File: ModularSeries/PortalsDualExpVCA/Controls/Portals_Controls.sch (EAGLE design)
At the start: 15 parts, among them SW1 SPDT_SWITCHDW1, SW2 SPDT_SWITCHDW1

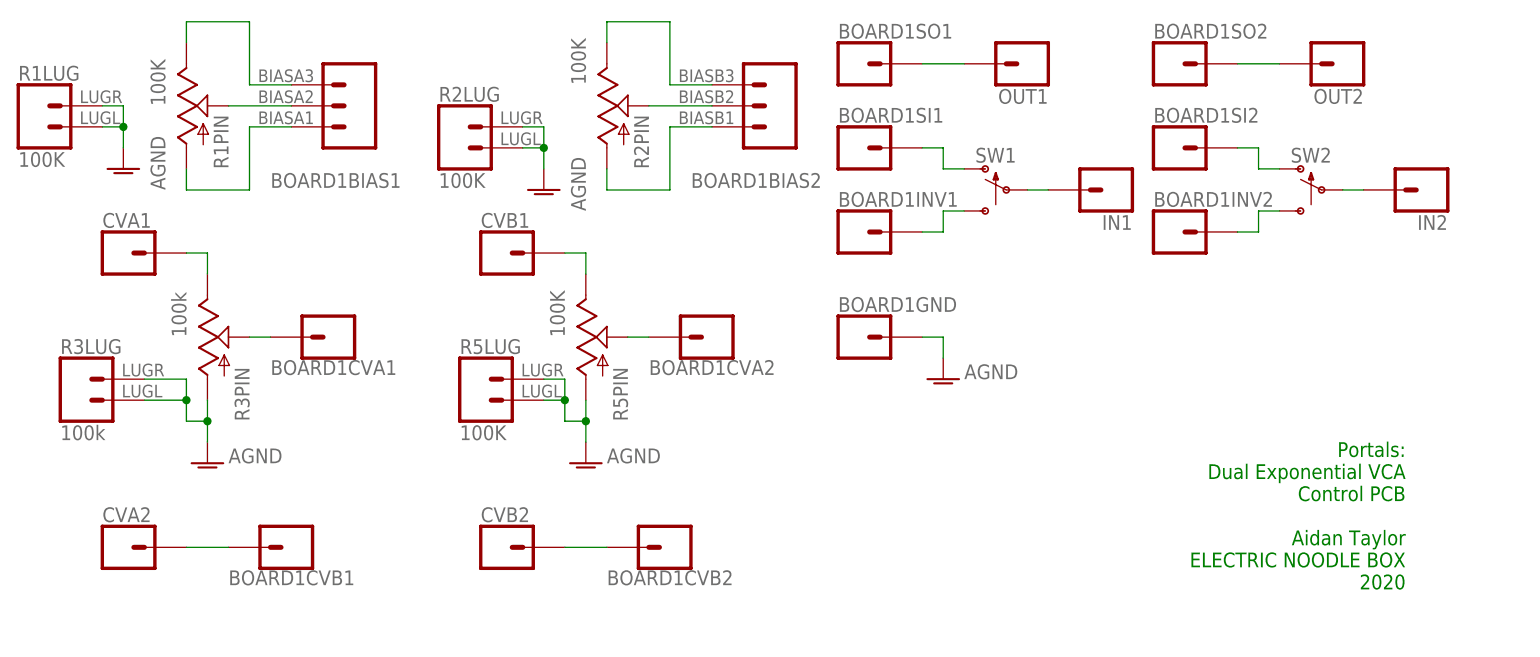
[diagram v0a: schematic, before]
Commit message: Pulse output fixed on Knives, schematics and layout updated. Panel added for Portals
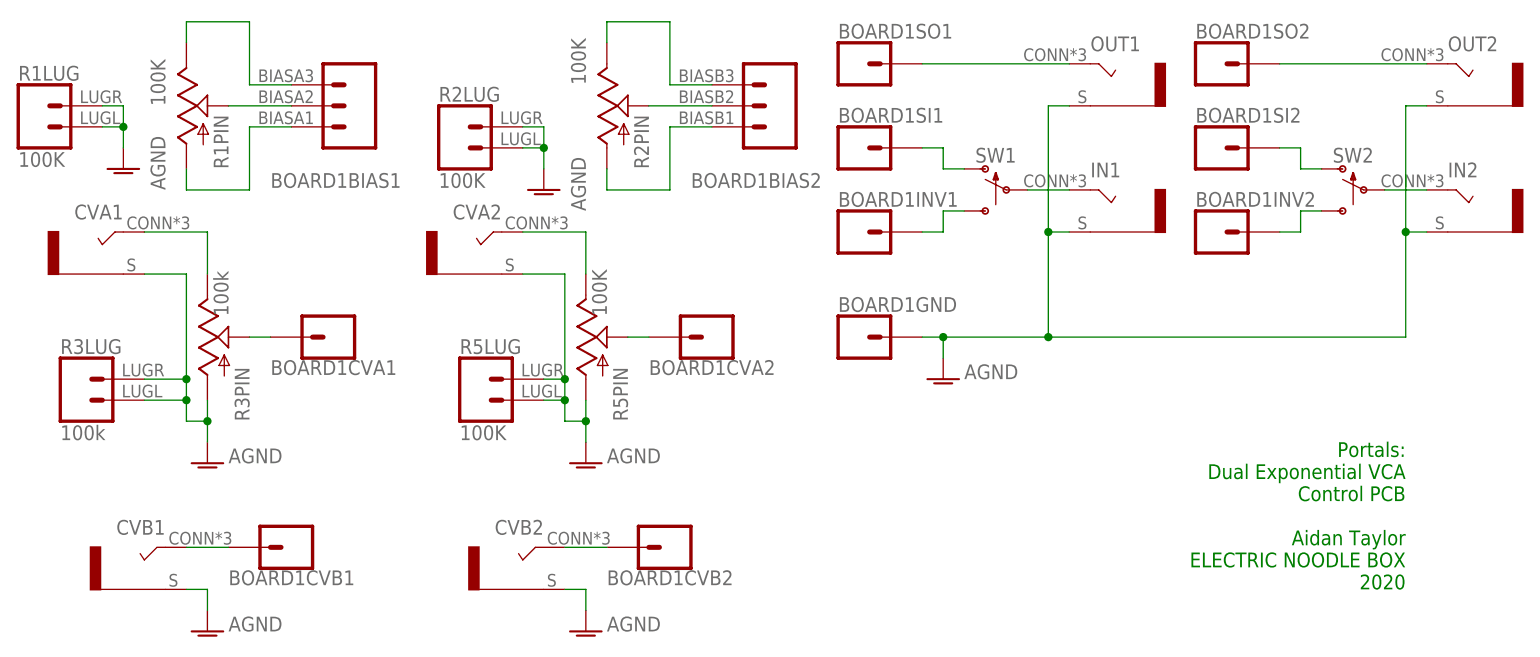
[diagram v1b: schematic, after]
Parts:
- CVA1, CVA2, CVB1, CVB2, IN1, IN2, OUT1, OUT2: value BANANA_PANEL -> COMBI-JACKCINCHNANA; device ElectricNoodleBox:BANANA_PANEL -> ElectricNoodleBox:COMBI-JACKCINCHNANA
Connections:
- net AGND: now also CVA1.S, CVA2.S, CVB1.S, CVB2.S, IN1.S, IN2.S, OUT1.S, OUT2.S
- net N$1: now also CVB1.T; no longer CVA2.1
- net N$11: now also CVA2.T; no longer CVB1.1
- net N$19: now also OUT2.T; no longer OUT2.1
- net N$2: now also CVB2.T; no longer CVB2.1
- net N$22: now also IN2.T; no longer IN2.1
- net N$3: now also CVA1.T; no longer CVA1.1
- net N$8: now also OUT1.T; no longer OUT1.1
- net N$9: now also IN1.T; no longer IN1.1
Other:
- moved on the sheet: BOARD1INV2, BOARD1SI2, BOARD1SO2, SW2

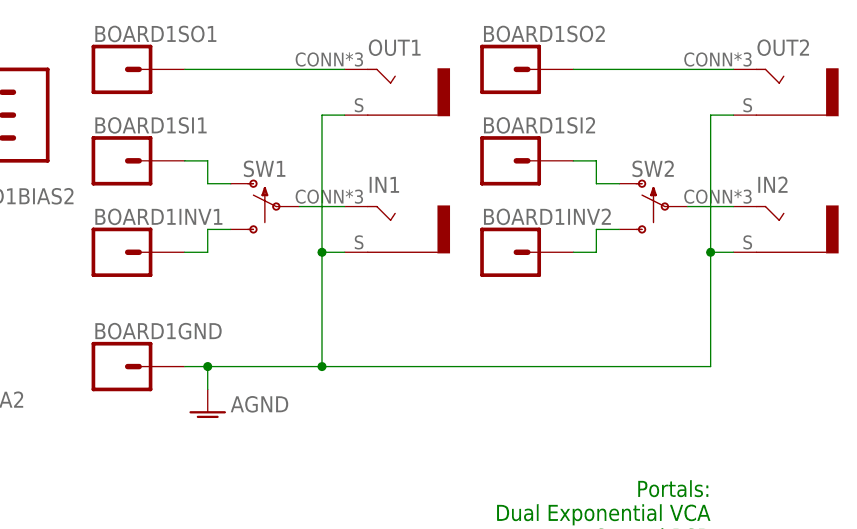
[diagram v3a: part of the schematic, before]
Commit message: Mirrors and Portals Renders brought up to date
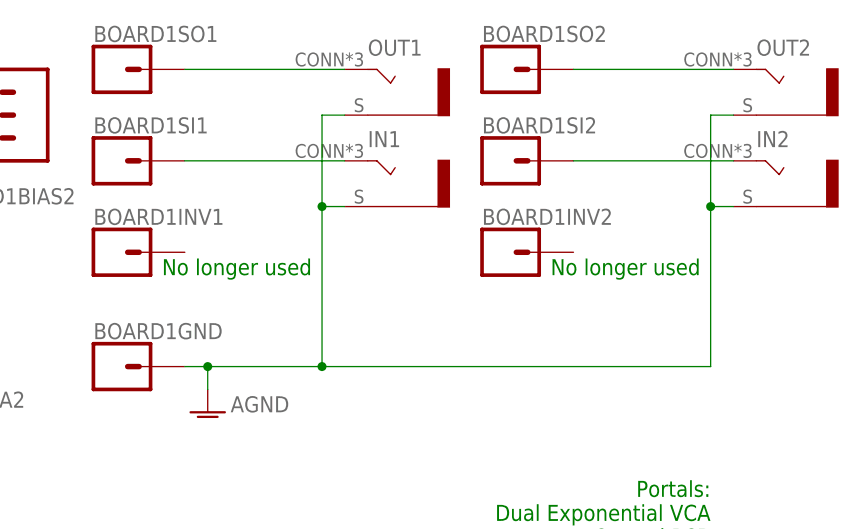
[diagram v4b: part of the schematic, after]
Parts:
- removed SW1, SW2: SPDT_SWITCHDW1, ElectricNoodleBox:SPDT_SWITCHDW1
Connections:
- removed net N$18: BOARD1INV1.1, SW1.S
- removed net N$20: BOARD1SI2.1, SW2.O
- removed net N$21: BOARD1INV2.1, SW2.S
- removed net N$22: IN2.T, SW2.P
- net N$10: now also BOARD1SI2.1, IN2.T; no longer BOARD1SI1.1, SW1.O
- net N$9: now also BOARD1SI1.1; no longer SW1.P
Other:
- note added: "No longer used"
- moved on the sheet: IN1, IN2
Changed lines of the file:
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@@
 <part name="AGND6" library="supply1" library_urn="urn:adsk.eagle:library:371" deviceset="AGND" device=""/>
 <part name="AGND7" library="supply1" library_urn="urn:adsk.eagle:library:371" deviceset="AGND" device=""/>
-<part name="SW1" library="ElectricNoodleBox" deviceset="SPDT_SWITCH" device="DW1"/>
-<part name="SW2" library="ElectricNoodleBox" deviceset="SPDT_SWITCH" device="DW1"/>
 <part name="CVA1" library="ElectricNoodleBox" deviceset="COMBI-JACK" device="CINCHNANA"/>
 <part name="CVB1" library="ElectricNoodleBox" deviceset="COMBI-JACK" device="CINCHNANA"/>
@@
 ELECTRIC NOODLE BOX
 2020</text>
+<text x="88.9" y="83.82" size="1.778" layer="91">No longer used</text>
+<text x="132.08" y="83.82" size="1.778" layer="91">No longer used</text>
 </plain>
 <instances>
@@
 <attribute name="VALUE" x="96.52" y="68.58" size="1.778" layer="96"/>
 </instance>
-<instance part="SW1" gate="G$1" x="99.06" y="91.44" smashed="yes" rot="MR0">
-<attribute name="NAME" x="100.33" y="94.742" size="1.778" layer="95" font="vector" rot="MR0" align="bottom-center"/>
-</instance>
-<instance part="SW2" gate="G$1" x="142.24" y="91.44" smashed="yes" rot="MR0">
-<attribute name="NAME" x="143.51" y="94.742" size="1.778" layer="95" font="vector" rot="MR0" align="bottom-center"/>
-</instance>
 <instance part="CVA1" gate="G$1" x="-7.62" y="83.82" smashed="yes" rot="MR0">
 <attribute name="NAME" x="-5.08" y="87.884" size="1.778" layer="95" rot="MR0"/>
@@
 <attribute name="NAME" x="111.76" y="108.204" size="1.778" layer="95"/>
 </instance>
-<instance part="IN1" gate="G$1" x="114.3" y="88.9" smashed="yes">
-<attribute name="NAME" x="111.76" y="92.964" size="1.778" layer="95"/>
+<instance part="IN1" gate="G$1" x="114.3" y="93.98" smashed="yes">
+<attribute name="NAME" x="111.76" y="98.044" size="1.778" layer="95"/>
 </instance>
 <instance part="OUT2" gate="G$1" x="157.48" y="104.14" smashed="yes">
 <attribute name="NAME" x="154.94" y="108.204" size="1.778" layer="95"/>
 </instance>
-<instance part="IN2" gate="G$1" x="157.48" y="88.9" smashed="yes">
-<attribute name="NAME" x="154.94" y="92.964" size="1.778" layer="95"/>
+<instance part="IN2" gate="G$1" x="157.48" y="93.98" smashed="yes">
+<attribute name="NAME" x="154.94" y="98.044" size="1.778" layer="95"/>
 </instance>
 </instances>
@@
 <pinref part="OUT1" gate="G$1" pin="S"/>
 <wire x1="109.22" y1="101.6" x2="106.68" y2="101.6" width="0.1524" layer="91"/>
-<wire x1="106.68" y1="101.6" x2="106.68" y2="86.36" width="0.1524" layer="91"/>
+<wire x1="106.68" y1="101.6" x2="106.68" y2="91.44" width="0.1524" layer="91"/>
 <pinref part="IN1" gate="G$1" pin="S"/>
-<wire x1="106.68" y1="86.36" x2="109.22" y2="86.36" width="0.1524" layer="91"/>
-<wire x1="106.68" y1="73.66" x2="106.68" y2="86.36" width="0.1524" layer="91"/>
-<junction x="106.68" y="86.36"/>
+<wire x1="106.68" y1="91.44" x2="109.22" y2="91.44" width="0.1524" layer="91"/>
+<wire x1="106.68" y1="73.66" x2="106.68" y2="91.44" width="0.1524" layer="91"/>
+<junction x="106.68" y="91.44"/>
 <wire x1="106.68" y1="73.66" x2="149.86" y2="73.66" width="0.1524" layer="91"/>
 <junction x="106.68" y="73.66"/>
 <pinref part="OUT2" gate="G$1" pin="S"/>
 <wire x1="152.4" y1="101.6" x2="149.86" y2="101.6" width="0.1524" layer="91"/>
-<wire x1="149.86" y1="101.6" x2="149.86" y2="86.36" width="0.1524" layer="91"/>
+<wire x1="149.86" y1="101.6" x2="149.86" y2="91.44" width="0.1524" layer="91"/>
 <pinref part="IN2" gate="G$1" pin="S"/>
-<wire x1="149.86" y1="86.36" x2="152.4" y2="86.36" width="0.1524" layer="91"/>
-<wire x1="149.86" y1="73.66" x2="149.86" y2="86.36" width="0.1524" layer="91"/>
-<junction x="149.86" y="86.36"/>
+<wire x1="149.86" y1="91.44" x2="152.4" y2="91.44" width="0.1524" layer="91"/>
+<wire x1="149.86" y1="73.66" x2="149.86" y2="91.44" width="0.1524" layer="91"/>
+<junction x="149.86" y="91.44"/>
 </segment>
 <segment>
@@
 </segment>
 </net>
-<net name="N$9" class="0">
-<segment>
-<pinref part="SW1" gate="G$1" pin="P"/>
-<pinref part="IN1" gate="G$1" pin="T"/>
-<wire x1="104.14" y1="91.44" x2="109.22" y2="91.44" width="0.1524" layer="91"/>
-</segment>
-</net>
-<net name="N$10" class="0">
-<segment>
-<pinref part="BOARD1" gate="SI1" pin="1"/>
-<wire x1="91.44" y1="96.52" x2="93.98" y2="96.52" width="0.1524" layer="91"/>
-<wire x1="93.98" y1="96.52" x2="93.98" y2="93.98" width="0.1524" layer="91"/>
-<pinref part="SW1" gate="G$1" pin="O"/>
-<wire x1="93.98" y1="93.98" x2="96.52" y2="93.98" width="0.1524" layer="91"/>
-</segment>
-</net>
-<net name="N$18" class="0">
-<segment>
-<pinref part="BOARD1" gate="INV1" pin="1"/>
-<wire x1="91.44" y1="86.36" x2="93.98" y2="86.36" width="0.1524" layer="91"/>
-<wire x1="93.98" y1="86.36" x2="93.98" y2="88.9" width="0.1524" layer="91"/>
-<pinref part="SW1" gate="G$1" pin="S"/>
-<wire x1="93.98" y1="88.9" x2="96.52" y2="88.9" width="0.1524" layer="91"/>
-</segment>
-</net>
 <net name="N$19" class="0">
 <segment>
@@
 </segment>
 </net>
-<net name="N$20" class="0">
-<segment>
-<pinref part="BOARD1" gate="SI2" pin="1"/>
-<wire x1="134.62" y1="96.52" x2="137.16" y2="96.52" width="0.1524" layer="91"/>
-<wire x1="137.16" y1="96.52" x2="137.16" y2="93.98" width="0.1524" layer="91"/>
-<pinref part="SW2" gate="G$1" pin="O"/>
-<wire x1="139.7" y1="93.98" x2="137.16" y2="93.98" width="0.1524" layer="91"/>
-</segment>
-</net>
-<net name="N$21" class="0">
-<segment>
-<pinref part="BOARD1" gate="INV2" pin="1"/>
-<wire x1="134.62" y1="86.36" x2="137.16" y2="86.36" width="0.1524" layer="91"/>
-<wire x1="137.16" y1="86.36" x2="137.16" y2="88.9" width="0.1524" layer="91"/>
-<pinref part="SW2" gate="G$1" pin="S"/>
-<wire x1="137.16" y1="88.9" x2="139.7" y2="88.9" width="0.1524" layer="91"/>
-</segment>
-</net>
-<net name="N$22" class="0">
-<segment>
-<pinref part="SW2" gate="G$1" pin="P"/>
-<pinref part="IN2" gate="G$1" pin="T"/>
-<wire x1="147.32" y1="91.44" x2="152.4" y2="91.44" width="0.1524" layer="91"/>
-</segment>
-</net>
 <net name="N$1" class="0">
 <segment>
@@
 </segment>
 </net>
+<net name="N$9" class="0">
+<segment>
+<pinref part="BOARD1" gate="SI1" pin="1"/>
+<pinref part="IN1" gate="G$1" pin="T"/>
+<wire x1="91.44" y1="96.52" x2="109.22" y2="96.52" width="0.1524" layer="91"/>
+</segment>
+</net>
+<net name="N$10" class="0">
+<segment>
+<pinref part="BOARD1" gate="SI2" pin="1"/>
+<pinref part="IN2" gate="G$1" pin="T"/>
+<wire x1="134.62" y1="96.52" x2="152.4" y2="96.52" width="0.1524" layer="91"/>
+</segment>
+</net>
